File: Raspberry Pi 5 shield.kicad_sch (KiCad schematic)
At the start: 34 parts, among them J1 Raspberry Connector, J2 Conn_02x02_Odd_Even, J3 DS1073-01-2x5-MVT6, U1 MCP2515-xSO, Y1 X322516MOB4SI

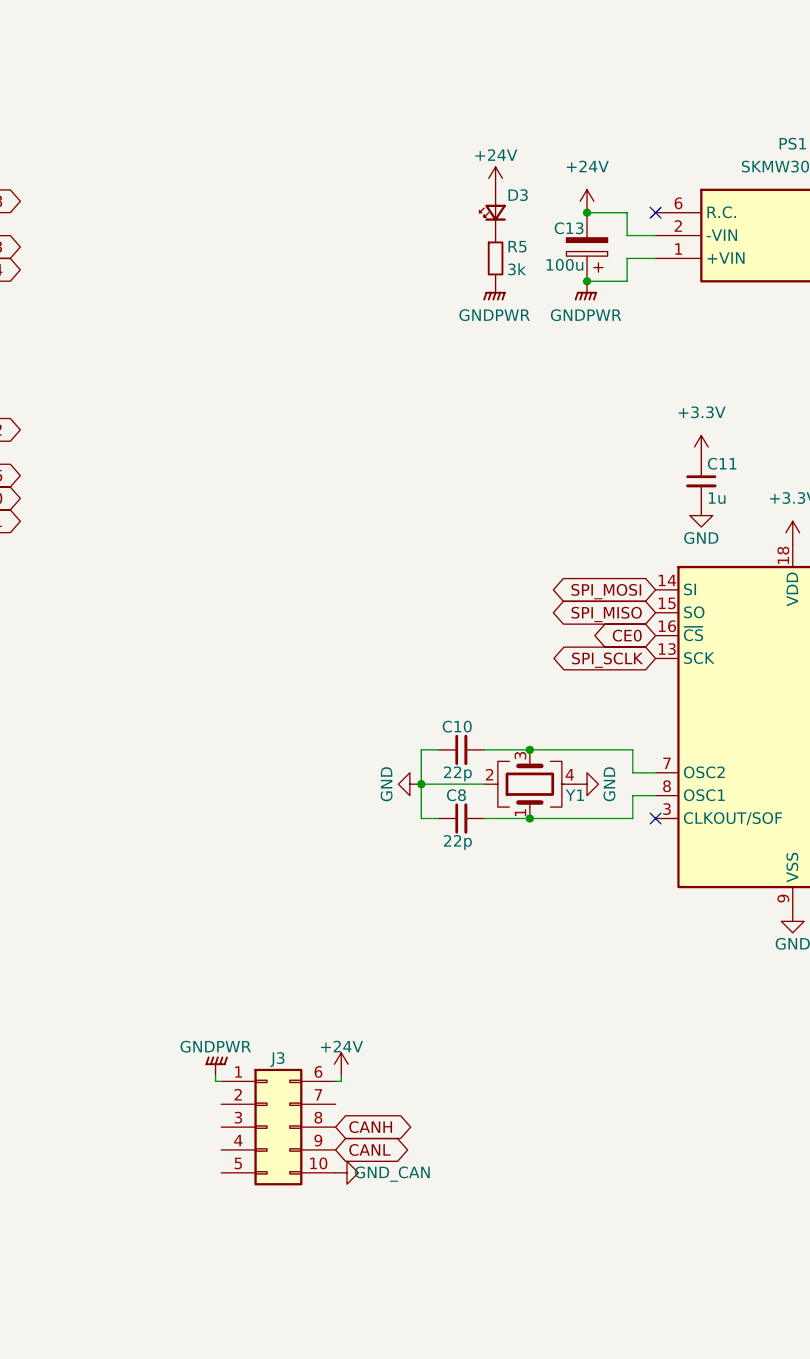
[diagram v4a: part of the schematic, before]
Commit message: Исправил косяки в схеме
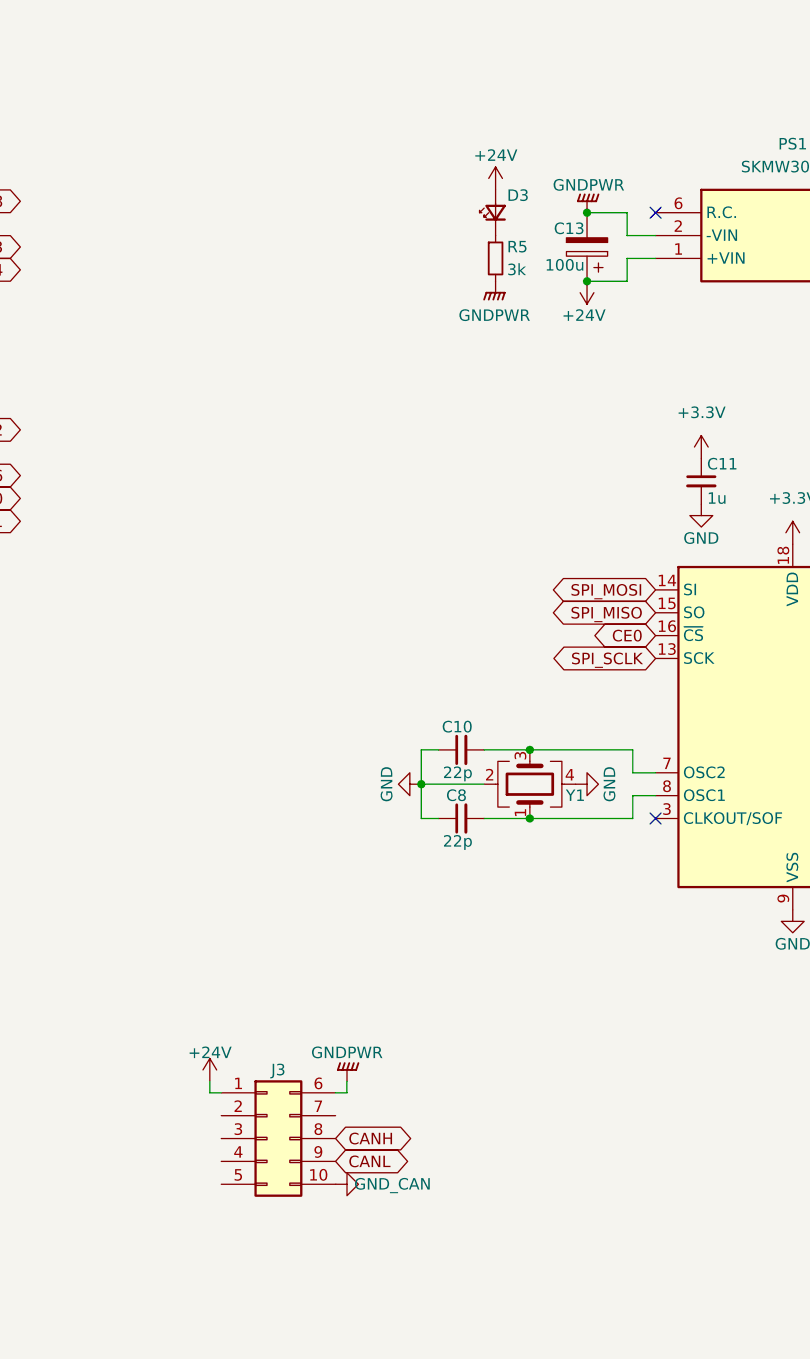
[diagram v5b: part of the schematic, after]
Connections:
- net +24V: now also C13.1, J3.1 (Pin_1), PS1.1 (+VIN); no longer C13.2, J3.6 (Pin_6), PS1.2 (-VIN)
- net GNDPWR: now also C13.2, J3.6 (Pin_6), PS1.2 (-VIN); no longer C13.1, J3.1 (Pin_1), PS1.1 (+VIN)
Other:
- moved on the sheet: J3
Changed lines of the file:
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@@
 	)
 	(junction
-		(at 116.84 50.8)
-		(diameter 0)
-		(color 0 0 0 0)
-	)
-	(junction
 		(at 193.04 80.01)
 		(diameter 0)
@@
 	)
 	(junction
+		(at 116.84 50.8)
+		(diameter 0)
+		(color 0 0 0 0)
+	)
+	(junction
 		(at 168.91 106.68)
 		(diameter 0)
@@
 	)
 	(junction
+		(at 116.84 43.18)
+		(diameter 0)
+		(color 0 0 0 0)
+	)
+	(junction
 		(at 158.75 40.64)
 		(diameter 0)
@@
 	)
 	(junction
-		(at 116.84 43.18)
-		(diameter 0)
-		(color 0 0 0 0)
-	)
-	(junction
 		(at 193.04 97.79)
 		(diameter 0)
@@
 	(wire
 		(pts
+			(xy 74.93 139.7) (xy 74.93 140.97)
+		)
+		(stroke
+			(width 0)
+			(type default)
+		)
+	)
+	(wire
+		(pts
 			(xy 158.75 40.64) (xy 167.64 40.64)
 		)
@@
 	(wire
 		(pts
+			(xy 74.93 140.97) (xy 76.2 140.97)
+		)
+		(stroke
+			(width 0)
+			(type default)
+		)
+	)
+	(wire
+		(pts
 			(xy 121.92 107.95) (xy 121.92 110.49)
 		)
@@
 	(wire
 		(pts
-			(xy 193.04 97.79) (xy 189.23 97.79)
+			(xy 90.17 139.7) (xy 90.17 140.97)
 		)
 		(stroke
@@
 	(wire
 		(pts
-			(xy 75.565 139.7) (xy 76.2 139.7)
+			(xy 193.04 97.79) (xy 189.23 97.79)
 		)
 		(stroke
@@
 	(wire
 		(pts
-			(xy 223.52 90.17) (xy 223.52 95.25)
+			(xy 90.17 140.97) (xy 88.9 140.97)
 		)
 		(stroke
@@
 	(wire
 		(pts
-			(xy 246.38 83.82) (xy 246.38 85.09)
+			(xy 223.52 90.17) (xy 223.52 95.25)
 		)
 		(stroke
@@
 	(wire
 		(pts
-			(xy 161.29 106.68) (xy 168.91 106.68)
+			(xy 246.38 83.82) (xy 246.38 85.09)
 		)
 		(stroke
@@
 	(wire
 		(pts
-			(xy 75.565 139.065) (xy 75.565 139.7)
+			(xy 161.29 106.68) (xy 168.91 106.68)
 		)
 		(stroke
@@
 	(wire
 		(pts
-			(xy 89.535 139.7) (xy 89.535 139.065)
-		)
-		(stroke
-			(width 0)
-			(type default)
-		)
-	)
-	(wire
-		(pts
 			(xy 154.94 43.18) (xy 154.94 40.64)
 		)
@@
 	(wire
 		(pts
-			(xy 88.9 139.7) (xy 89.535 139.7)
-		)
-		(stroke
-			(width 0)
-			(type default)
-		)
-	)
-	(wire
-		(pts
 			(xy 189.23 102.87) (xy 193.04 102.87)
 		)
@@
 	(global_label "CANL"
 		(shape bidirectional)
-		(at 88.9 147.32 0)
+		(at 88.9 148.59 0)
 		(fields_autoplaced yes)
 		(effects
@@
 		)
 		(property "Intersheetrefs" "${INTERSHEET_REFS}"
-			(at 96.7147 147.32 0)
+			(at 96.7147 148.59 0)
 			(effects
 				(font
@@
 	(global_label "CANH"
 		(shape bidirectional)
-		(at 88.9 144.78 0)
+		(at 88.9 146.05 0)
 		(fields_autoplaced yes)
 		(effects
@@
 		)
 		(property "Intersheetrefs" "${INTERSHEET_REFS}"
-			(at 96.8425 144.78 0)
+			(at 96.8425 146.05 0)
 			(effects
 				(font
@@
 	(symbol
 		(lib_id "power:GNDPWR")
-		(at 116.84 50.8 0)
+		(at 116.84 43.18 180)
 		(unit 1)
 		(exclude_from_sim no)
@@
 		(on_board yes)
 		(dnp no)
-		(fields_autoplaced yes)
 		(property "Reference" "#PWR041"
-			(at 116.84 55.88 0)
+			(at 116.84 38.1 0)
 			(effects
 				(font
@@
 		)
 		(property "Value" "GNDPWR"
-			(at 116.713 54.61 0)
+			(at 113.03 40.132 0)
 			(effects
 				(font
 					(size 1.27 1.27)
 				)
+				(justify right)
 			)
 		)
 		(property "Footprint" ""
-			(at 116.84 52.07 0)
+			(at 116.84 41.91 0)
 			(effects
 				(font
@@
 		)
 		(property "Datasheet" ""
-			(at 116.84 52.07 0)
+			(at 116.84 41.91 0)
 			(effects
 				(font
@@
 		)
 		(property "Description" "Power symbol creates a global label with name \"GNDPWR\" , global ground"
-			(at 116.84 50.8 0)
+			(at 116.84 43.18 0)
 			(effects
 				(font
@@
 	(symbol
 		(lib_id "Connector_Generic:Conn_02x05_Top_Bottom")
-		(at 81.28 144.78 0)
+		(at 81.28 146.05 0)
 		(unit 1)
 		(exclude_from_sim no)
@@
 		(dnp no)
 		(property "Reference" "J3"
-			(at 82.55 137.16 0)
+			(at 82.55 138.43 0)
 			(effects
 				(font
@@
 		)
 		(property "Value" "DS1073-01-2x5-MVT6"
-			(at 82.55 135.89 0)
+			(at 82.55 137.16 0)
 			(effects
 				(font
@@
 		)
 		(property "Footprint" "Molex_My:MIni-Fit_02x05_Vertical"
-			(at 81.28 144.78 0)
+			(at 81.28 146.05 0)
 			(effects
 				(font
@@
 		)
 		(property "Datasheet" "https://www.chipdip.ru/product/ds1073-01-2x5-mvt6-mf2x5ma"
-			(at 81.28 144.78 0)
+			(at 81.28 146.05 0)
 			(effects
 				(font
@@
 		)
 		(property "Description" "Generic connector, double row, 02x05, top/bottom pin numbering scheme (row 1: 1...pins_per_row, row2: pins_per_row+1 ... num_pins), script generated (kicad-library-utils/schlib/autogen/connector/)"
-			(at 81.28 144.78 0)
+			(at 81.28 146.05 0)
 			(effects
 				(font
@@
 		)
 		(property "Deadline" ""
-			(at 81.28 144.78 0)
+			(at 81.28 146.05 0)
 			(effects
 				(font
@@
 		)
 		(property "Manufacturer" ""
-			(at 81.28 144.78 0)
+			(at 81.28 146.05 0)
 			(effects
 				(font
@@
 		)
 		(property "Name" "DS1073-01-2x5-MVT6"
-			(at 81.28 144.78 0)
+			(at 81.28 146.05 0)
 			(effects
 				(font
@@
 		)
 		(property "Part number" ""
-			(at 81.28 144.78 0)
+			(at 81.28 146.05 0)
 			(effects
 				(font
@@
 		)
 		(property "Quantity for order" ""
-			(at 81.28 144.78 0)
+			(at 81.28 146.05 0)
 			(effects
 				(font
@@
 	(symbol
 		(lib_id "power:+24V")
-		(at 116.84 43.18 0)
+		(at 116.84 50.8 180)
 		(unit 1)
 		(exclude_from_sim no)
@@
 		(on_board yes)
 		(dnp no)
-		(fields_autoplaced yes)
 		(property "Reference" "#PWR042"
 			(at 116.84 46.99 0)
@@
 		)
 		(property "Value" "+24V"
-			(at 116.84 38.1 0)
+			(at 114.046 54.61 0)
 			(effects
 				(font
 					(size 1.27 1.27)
 				)
+				(justify right)
 			)
 		)
 		(property "Footprint" ""
-			(at 116.84 43.18 0)
+			(at 116.84 50.8 0)
 			(effects
 				(font
@@
 		)
 		(property "Datasheet" ""
-			(at 116.84 43.18 0)
+			(at 116.84 50.8 0)
 			(effects
 				(font
@@
 		)
 		(property "Description" "Power symbol creates a global label with name \"+24V\""
-			(at 116.84 43.18 0)
+			(at 116.84 50.8 0)
 			(effects
 				(font
@@
 	(symbol
 		(lib_id "Power_My:GND_CAN")
-		(at 88.9 149.86 90)
+		(at 88.9 151.13 90)
 		(unit 1)
 		(exclude_from_sim no)
@@
 		(dnp no)
 		(property "Reference" "#PWR045"
-			(at 94.488 149.86 0)
+			(at 94.488 151.13 0)
 			(effects
 				(font
@@
 		)
 		(property "Value" "GND_CAN"
-			(at 95.25 149.86 90)
+			(at 95.25 151.13 90)
 			(effects
 				(font
@@
 		)
 		(property "Footprint" ""
-			(at 88.9 149.86 0)
+			(at 88.9 151.13 0)
 			(effects
 				(font
@@
 		)
 		(property "Datasheet" ""
-			(at 88.9 149.86 0)
+			(at 88.9 151.13 0)
 			(effects
 				(font
@@
 		)
 		(property "Description" "Power symbol creates a global label with name \"GND_CAN\" , ground"
-			(at 88.9 149.86 0)
+			(at 88.9 151.13 0)
 			(effects
 				(font
@@
 	(symbol
 		(lib_id "power:+24V")
-		(at 89.535 139.065 0)
+		(at 74.93 139.7 0)
 		(unit 1)
 		(exclude_from_sim no)
@@
 		(dnp no)
 		(property "Reference" "#PWR043"
-			(at 89.535 142.875 0)
+			(at 74.93 143.51 0)
 			(effects
 				(font
@@
 		)
 		(property "Value" "+24V"
-			(at 89.535 135.89 0)
+			(at 74.93 136.525 0)
 			(effects
 				(font
@@
 		)
 		(property "Footprint" ""
-			(at 89.535 139.065 0)
+			(at 74.93 139.7 0)
 			(effects
 				(font
@@
 		)
 		(property "Datasheet" ""
-			(at 89.535 139.065 0)
+			(at 74.93 139.7 0)
 			(effects
 				(font
@@
 		)
 		(property "Description" "Power symbol creates a global label with name \"+24V\""
-			(at 89.535 139.065 0)
+			(at 74.93 139.7 0)
 			(effects
 				(font
@@
 	(symbol
 		(lib_id "power:GNDPWR")
-		(at 75.565 139.065 180)
+		(at 90.17 139.7 180)
 		(unit 1)
 		(exclude_from_sim no)
@@
 		(dnp no)
 		(property "Reference" "#PWR044"
-			(at 75.565 133.985 0)
+			(at 90.17 134.62 0)
 			(effects
 				(font
@@
 		)
 		(property "Value" "GNDPWR"
-			(at 75.565 135.89 0)
+			(at 90.17 136.525 0)
 			(effects
 				(font
@@
 		)
 		(property "Footprint" ""
-			(at 75.565 137.795 0)
+			(at 90.17 138.43 0)
 			(effects
 				(font
@@
 		)
 		(property "Datasheet" ""
-			(at 75.565 137.795 0)
+			(at 90.17 138.43 0)
 			(effects
 				(font
@@
 		)
 		(property "Description" "Power symbol creates a global label with name \"GNDPWR\" , global ground"
-			(at 75.565 139.065 0)
+			(at 90.17 139.7 0)
 			(effects
 				(font
